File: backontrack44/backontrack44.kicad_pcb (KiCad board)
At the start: 2 copper layers, 153.7 x 95.6 mm, 98 parts, among them J1 AudioJack4, J2 OLED, SW1-1 choc_SW_HS, SW1-2 choc_SW_HS, SW1-3 choc_SW_HS, SW1-4 choc_SW_HS, SW1-5 choc_SW_HS, SW1-6 choc_SW_HS, SW2-1 choc_SW_HS, SW2-2 choc_SW_HS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

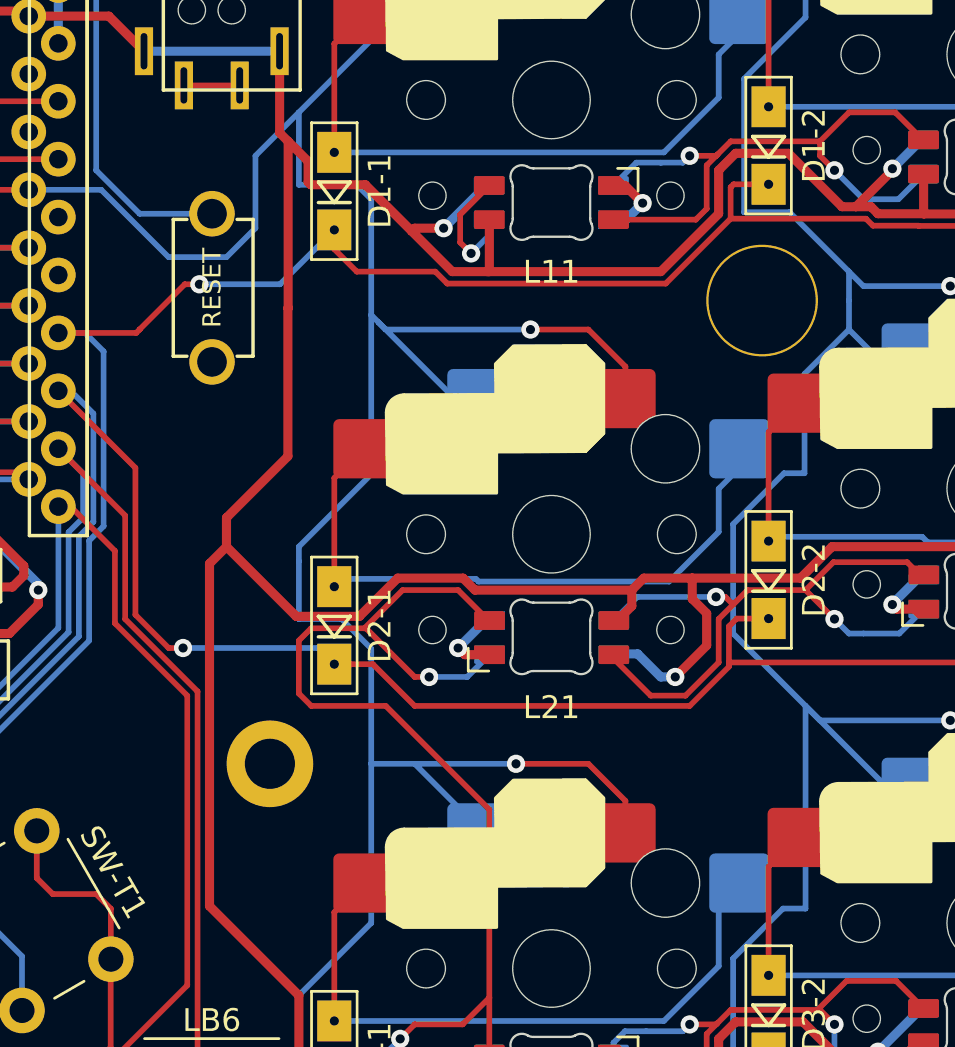
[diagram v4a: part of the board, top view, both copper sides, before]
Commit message: fixed another DRC error
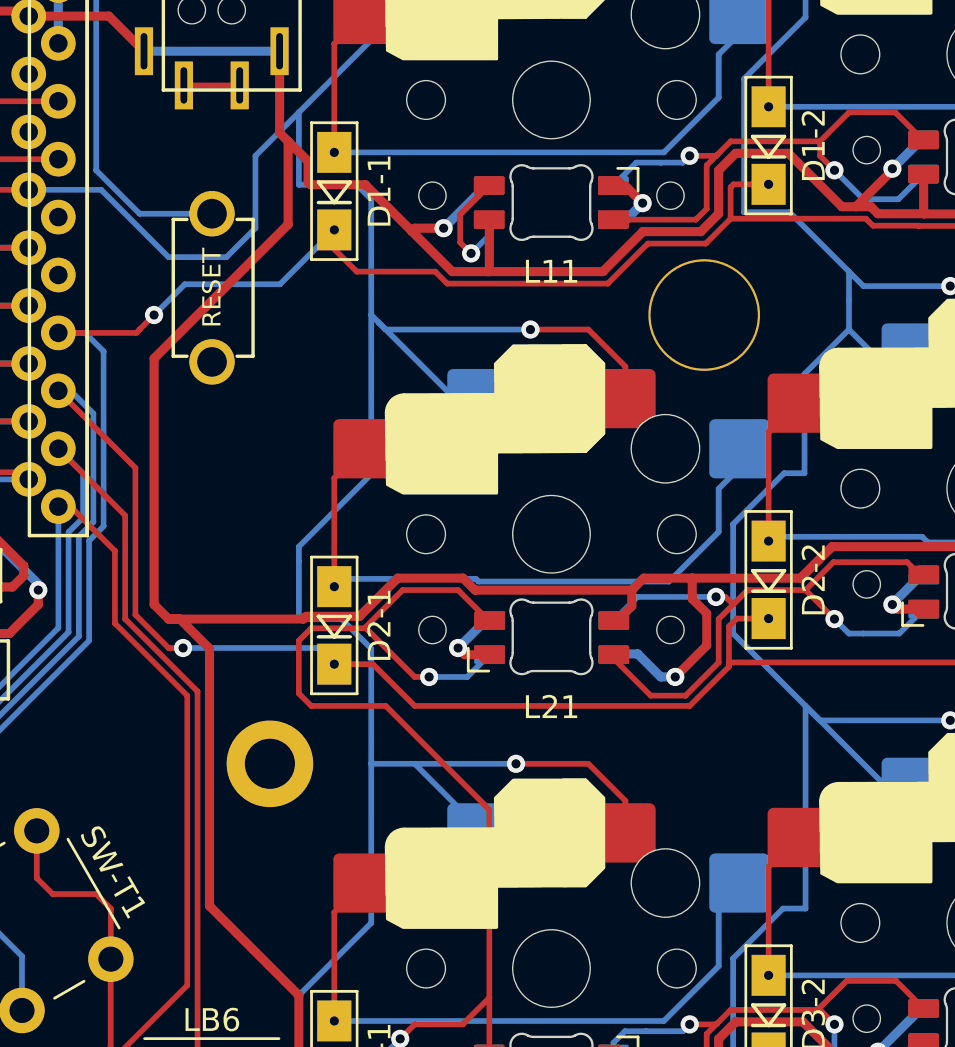
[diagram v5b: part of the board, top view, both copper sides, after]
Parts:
- moved H8 2.62 mm to (101.6, 51.4)
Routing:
- net VCC: track 763.7 -> 767.3 mm

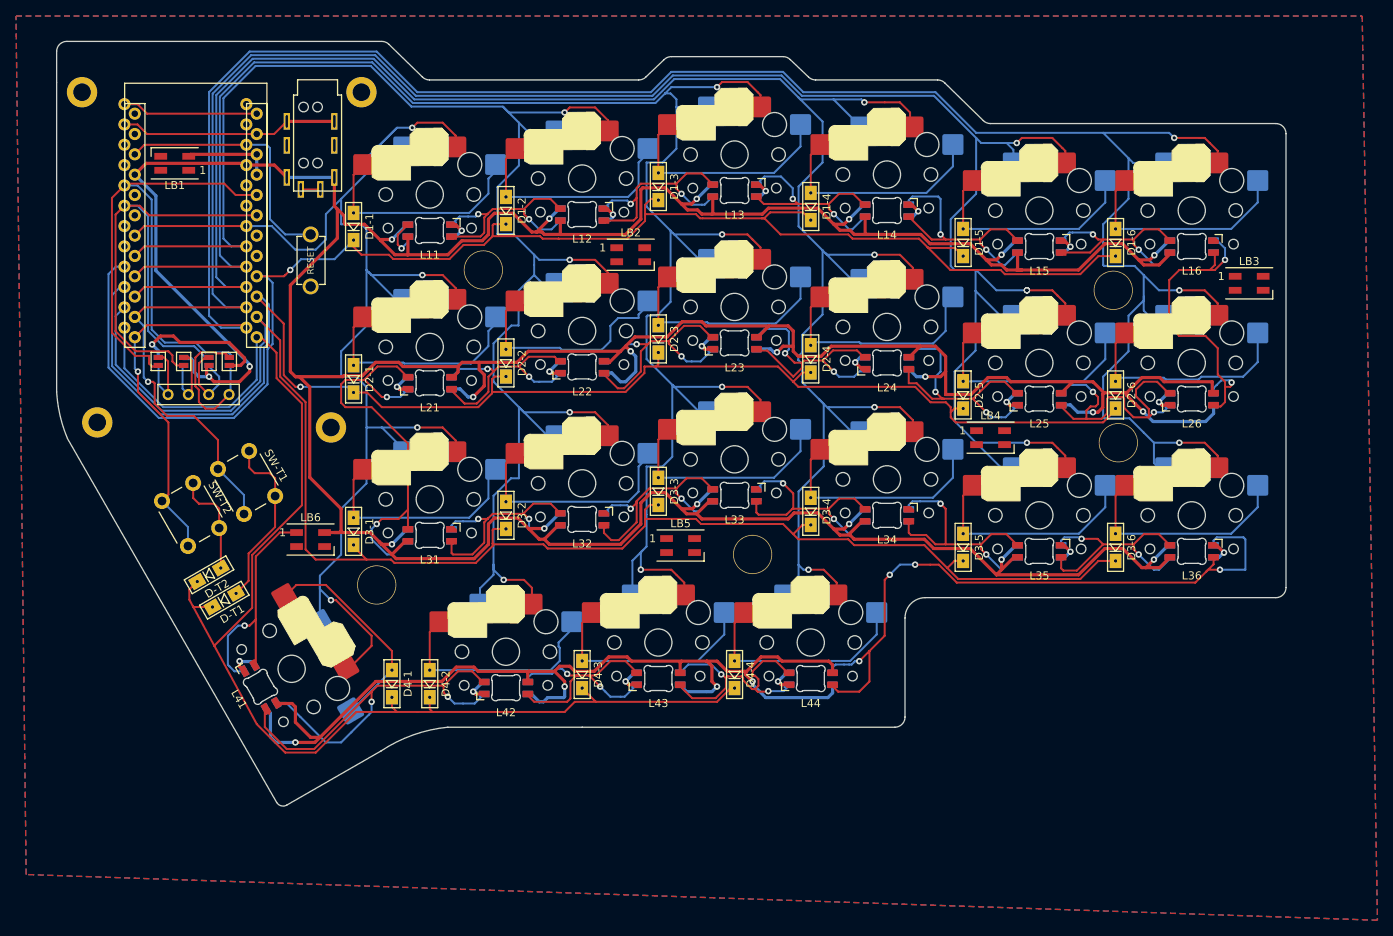
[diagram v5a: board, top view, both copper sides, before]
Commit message: fixed another DRC error
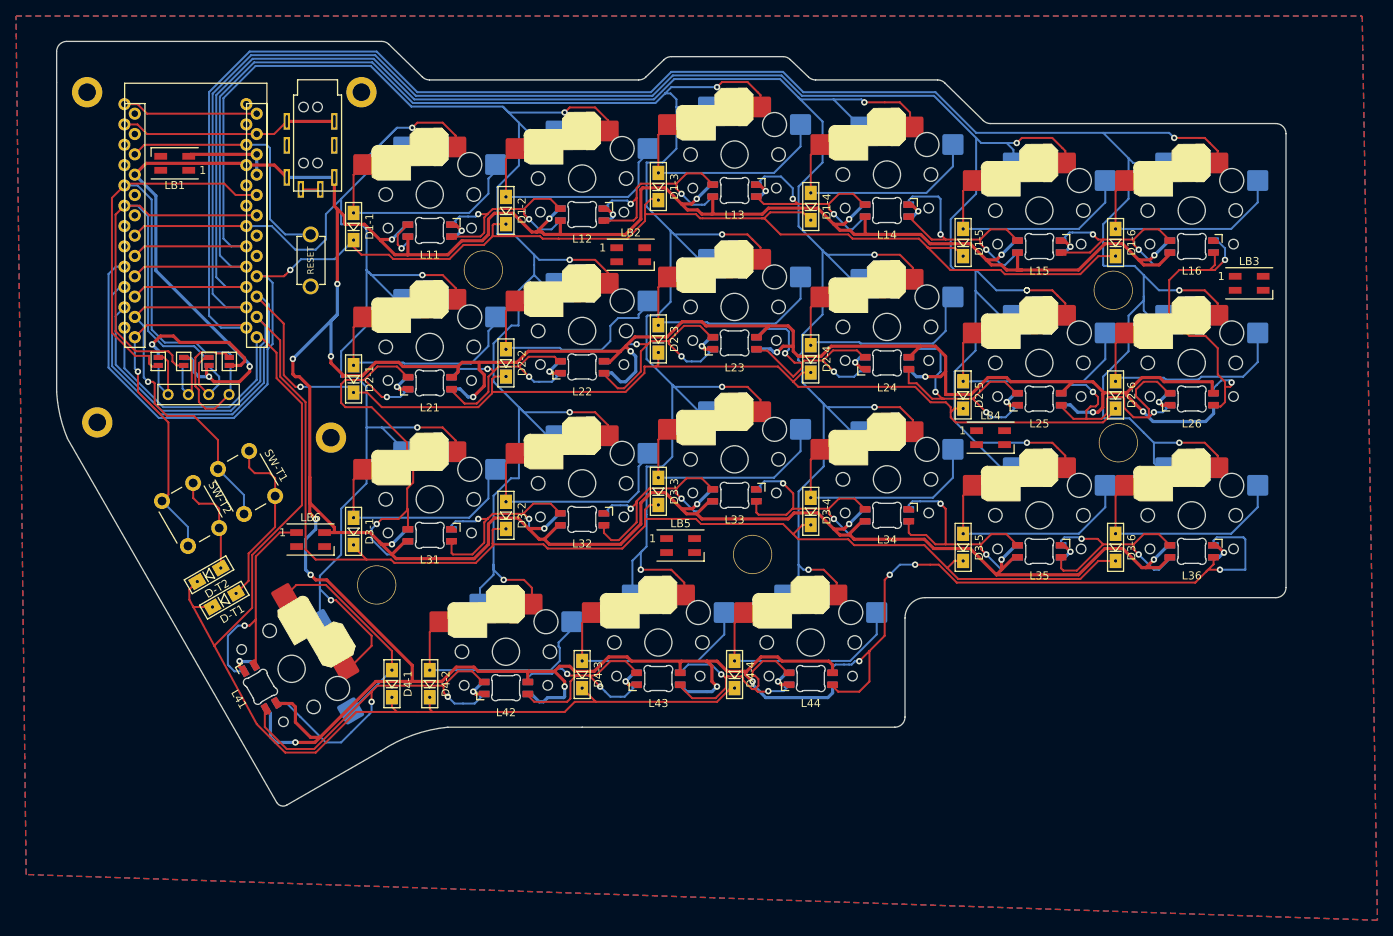
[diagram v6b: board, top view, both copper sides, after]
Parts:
- moved H3 1.27 mm to (82.5, 72.4)
- moved H4 0.63 mm to (52.1, 29.2)
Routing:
- net VCC: track 767.3 -> 801.4 mm, vias 24 -> 29
- net Net-(L16-Pad3): track 40.2 -> 39.5 mm
- net Net-(L21-Pad3): track 53.1 -> 53.7 mm
